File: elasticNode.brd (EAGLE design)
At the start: 82.2 x 52.5 mm, 101 parts, among them J1 ISP_CONN_6PIN, J2 FEMALE_HEADER_2X2, J3 FEMALE_HEADER_2X1, J4 FEMALE_HEADER_2X1, J5 FEMALE_HEADER_5X2, J6 FEMALE_HEADER_5X2, J7 JTAG_CONN_6PINTHT, J8 USB_CONN, U1 ATMEGA64AQFN, U10 LTC3419DFN, U2 SST26VF032B, U3 MRF24J40MA, U4 SPARTAN6-LX9, U5 SST26VF032B, U6 PAC1720, U7 PAC1720, U8 PAC1720, U9 FT232R, X1 12MHz, X2 50MHz, X3 32MHz

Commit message: changed i2c to pullup
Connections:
- removed net N$33: R25.2
- net 3V3: now also R24.2, R25.2
- net GND: no longer R24.2

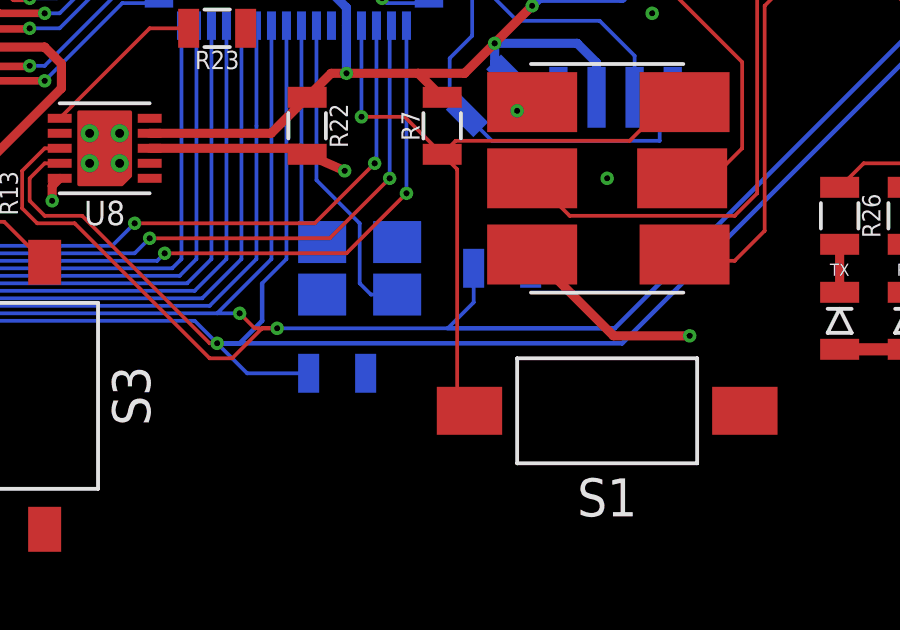
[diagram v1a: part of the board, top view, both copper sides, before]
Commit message: updated board for previous pullups and swapped fpga power rails
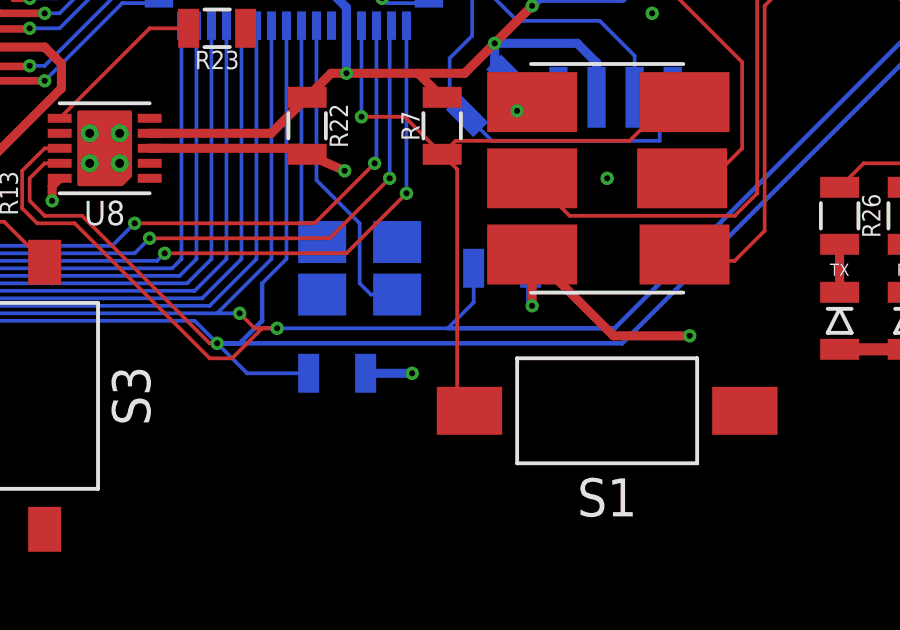
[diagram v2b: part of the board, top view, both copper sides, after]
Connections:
- net 1V2: now also R17.2, U7.3; no longer R19.2, U7.1
- net 3V3: now also R19.2, U7.1; no longer R17.2, U7.3
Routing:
- net 3V3: track 37.6 -> 45.4 mm, vias 11 -> 13
- net 1V2: track 61.3 -> 59.4 mm

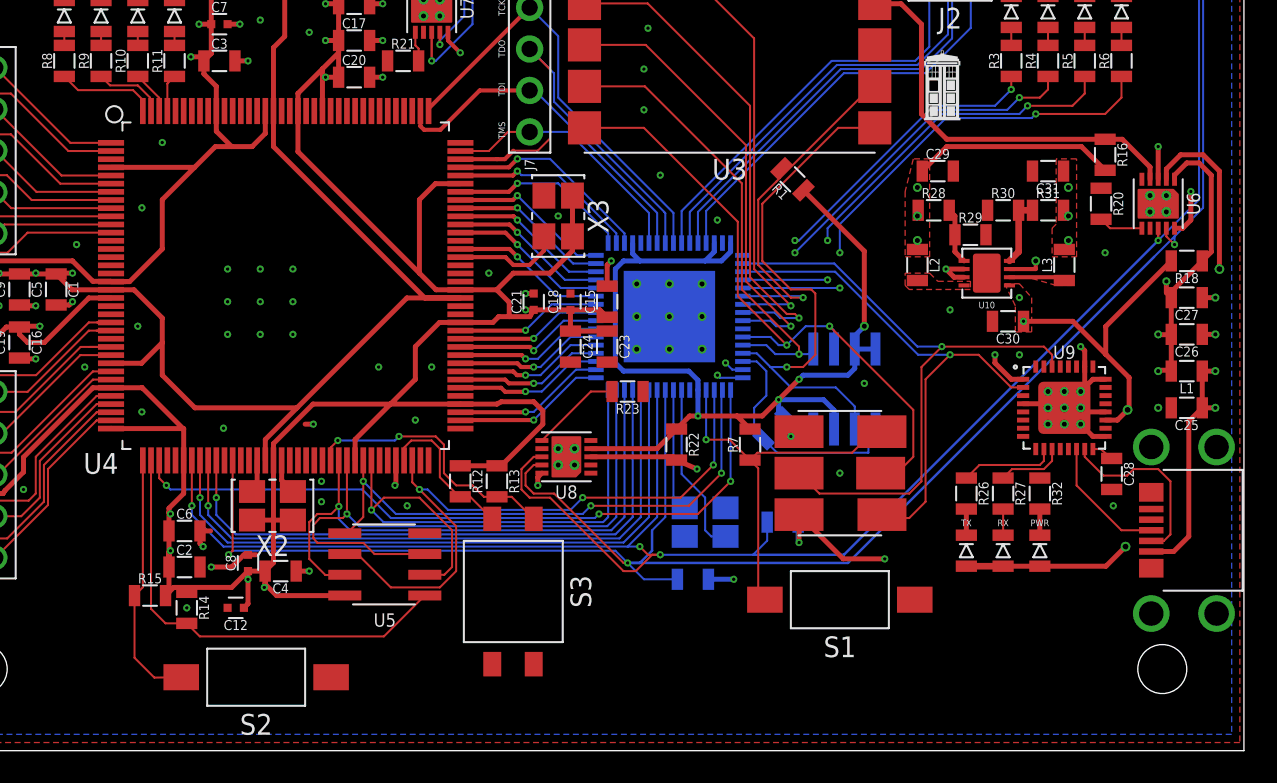
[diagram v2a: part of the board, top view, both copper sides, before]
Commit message: added smd usb connector
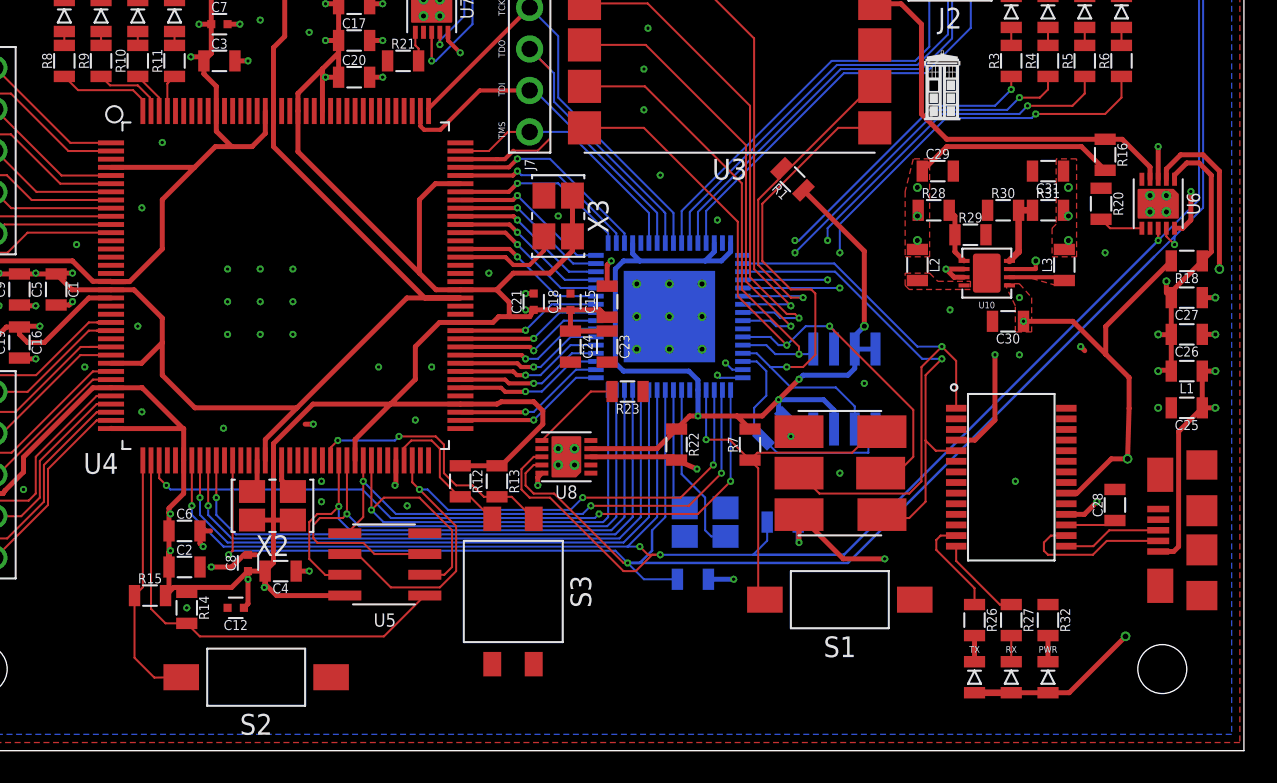
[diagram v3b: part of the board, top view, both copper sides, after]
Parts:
- J8: value USB_CONN -> USB_CONNSMT; device connectors:USB_MICRO_B -> connectors:USB_MICRO_B_SMT
- U9: value FT232R -> FT232RSSOP28; device ic:QFN32 -> ic:SSOP28
- moved PWR 7.77 mm to (70.2, 4.50)
- moved R26 7.77 mm to (65.8, 8.00)
- moved R27 7.77 mm to (68.0, 8.00)
- moved R32 7.77 mm to (70.2, 8.00)
- moved RX 7.77 mm to (68.0, 4.50)
- moved TX 7.77 mm to (65.8, 4.50)
- moved U9 5.35 mm to (68.0, 16.8), turned to 270 degrees
- moved J8 2.75 mm to (77.0, 13.5)
- moved C28 1.91 mm to (74.3, 15.1), turned to 90 degrees
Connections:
- removed net N$17 (its old number): U9.32
- new net N$26: U9.12
- net 12MHZ: now also U9.23; no longer U9.22
- net 5V: now also U9.20, U9.4; no longer U9.1, U9.19
- net FTDI_RXLED: now also U9.14; no longer U9.11
- net GND: now also U9.18, U9.21, U9.25, U9.7; no longer U9.17, U9.20, U9.24, U9.33, U9.4, U9.P$1, U9.P$2, U9.P$3, U9.P$4, U9.P$5, U9.P$6, U9.P$7, U9.P$8, U9.P$9
- net MCU_RX0/PDI: now also U9.1; no longer U9.30
- net MCU_TX0/PDO: now also U9.5; no longer U9.2
- net N$10: now also U9.13; no longer U9.10
- net N$18: now also U9.11; no longer U9.8
- net N$19: now also U9.2; no longer U9.31
- net N$21: now also U9.10; no longer U9.7
- net N$3: now also U9.17; no longer U9.16
- net N$6: now also U9.19; no longer U9.18
- net USBD+: now also U9.15; no longer U9.14
- net USBD-: now also U9.16; no longer U9.15
- net USB_SHIELD: now also J8.CASE_1; no longer J8.SHIELD1
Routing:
- net 5V: track 74.6 -> 87.8 mm
- net GND: track 34.4 -> 26.0 mm, vias 68 -> 69
- net MCU_TX0/PDO: track 32.9 -> 28.9 mm
- net MCU_RX0/PDI: track 39.1 -> 35.5 mm
- net USBD+: track 7.94 -> 6.03 mm
- net USBD-: track 11.3 -> 9.51 mm
- net N$3: track 1.36 -> 3.09 mm
- net FTDI_RXLED: track 4.16 -> 5.38 mm

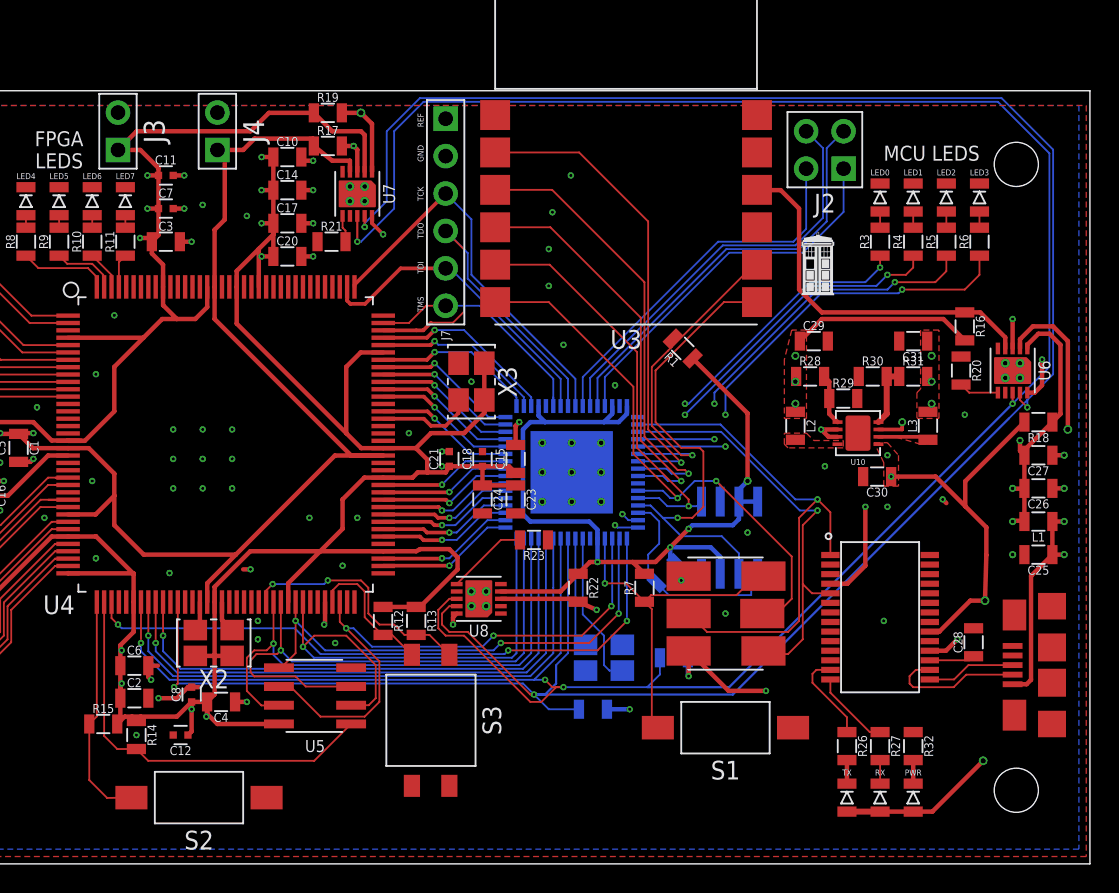
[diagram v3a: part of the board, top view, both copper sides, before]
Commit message: updated footprints, moved reset buttons, general reorganising
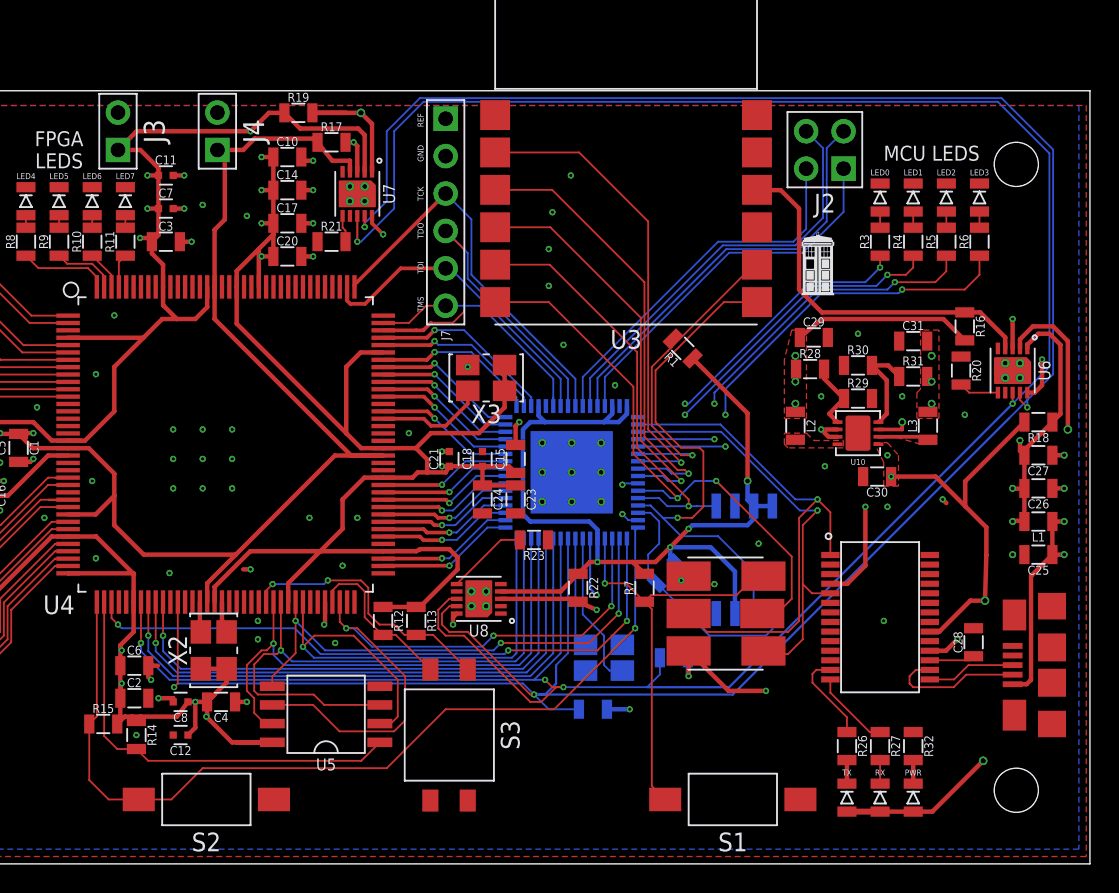
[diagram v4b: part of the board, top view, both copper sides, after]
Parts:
- moved S1 4.90 mm to (58.0, 4.38)
- moved R19 2.00 mm to (28.5, 51.0)
- moved U2 1.80 mm to (58.8, 20.6)
- moved S3 1.60 mm to (38.8, 8.75)
- moved U5 1.46 mm to (30.4, 10.2)
- moved R30 1.25 mm to (66.5, 33.9)
- moved X3 1.03 mm to (41.2, 33.0), turned to 180 degrees
- moved R29 1.00 mm to (66.5, 31.6)
- moved C8 0.90 mm to (20.5, 11.0), turned to 180 degrees
- moved S2 0.52 mm to (22.2, 4.38)
- moved R28 0.50 mm to (63.2, 33.6)
- moved X2 0.50 mm to (22.8, 14.5), turned to 90 degrees
- moved R17 0.35 mm to (30.8, 49.0)
- moved C29 0.25 mm to (63.5, 35.8)
- turned C31 to 0 degrees
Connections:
- removed net MCU_CS: U1.10
- removed net N$38: U1.23, X1.2
- removed net N$39: U1.24, X1.4
- new net XTAL1: U1.24, X1.3
- new net XTAL2: U1.23, X1.1
- net 1V2: now also C31.2; no longer C31.1
- net FPGA_RESET: now also U1.16
- net GND: now also C31.1; no longer C31.2
- net MCU_LED0: now also U1.15; no longer U1.16
- net MCU_LED1: now also U1.10; no longer U1.15
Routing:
- net FPGA_RESET: track 15.7 -> 61.6 mm, vias 0 -> 1
- net XTAL2: track 0.00 -> 10.6 mm
- net N$38: track 10.6 -> 0.00 mm
- net XTAL1: track 0.00 -> 7.50 mm
- net N$39: track 7.50 -> 0.00 mm
- net MCU_RESET: track 24.0 -> 29.1 mm
- net CCLK: track 40.2 -> 44.7 mm
- net MCU_VCC: track 63.4 -> 67.5 mm
- net 3V3: track 45.4 -> 49.2 mm
- net MCU_MISO: track 32.8 -> 35.8 mm
- net SELECTMAP_D1/FPGA_MISO2: track 38.5 -> 41.0 mm
- net N$7: track 4.18 -> 6.66 mm
- net MCU_FLASH_CE: track 14.8 -> 17.0 mm
- net MCU_LED1: track 30.2 -> 28.0 mm
- net GND: track 26.0 -> 28.1 mm, vias 69 -> 73
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
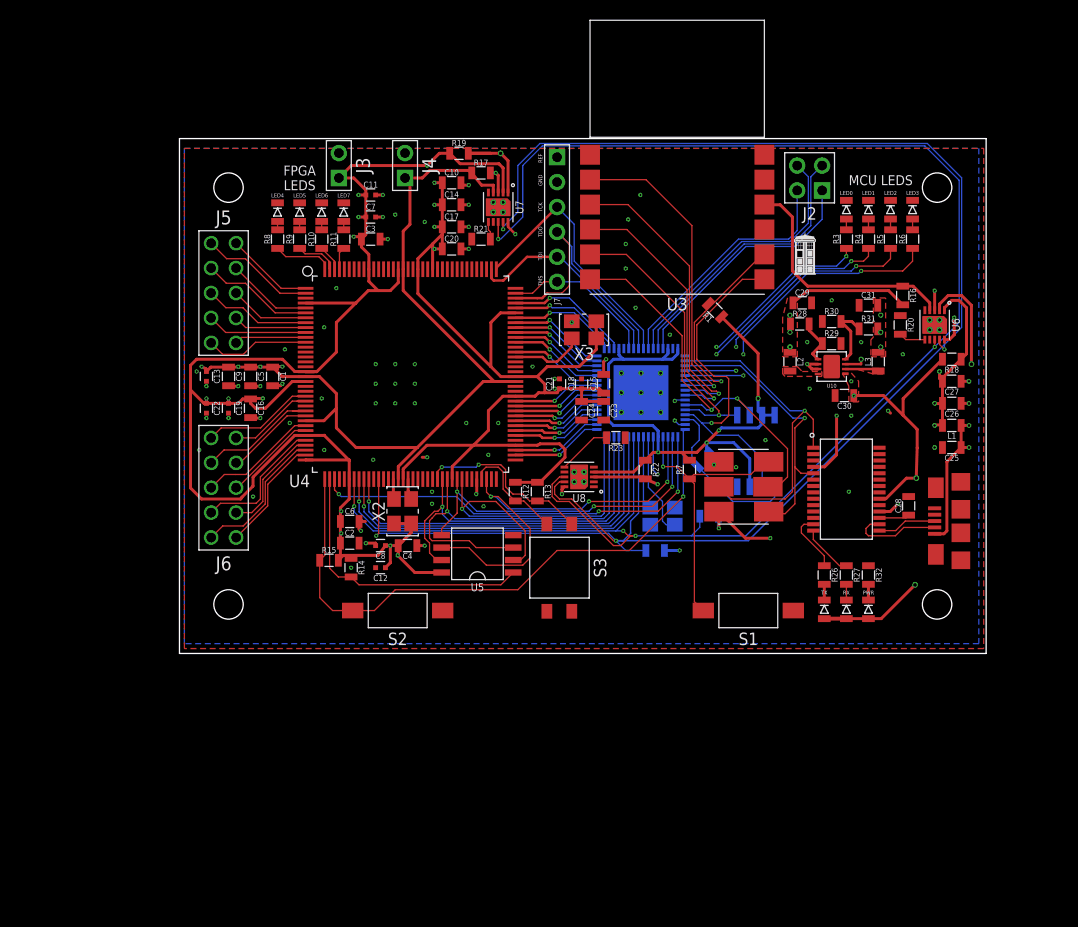
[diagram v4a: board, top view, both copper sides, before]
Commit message: first part toward separate monitoring board
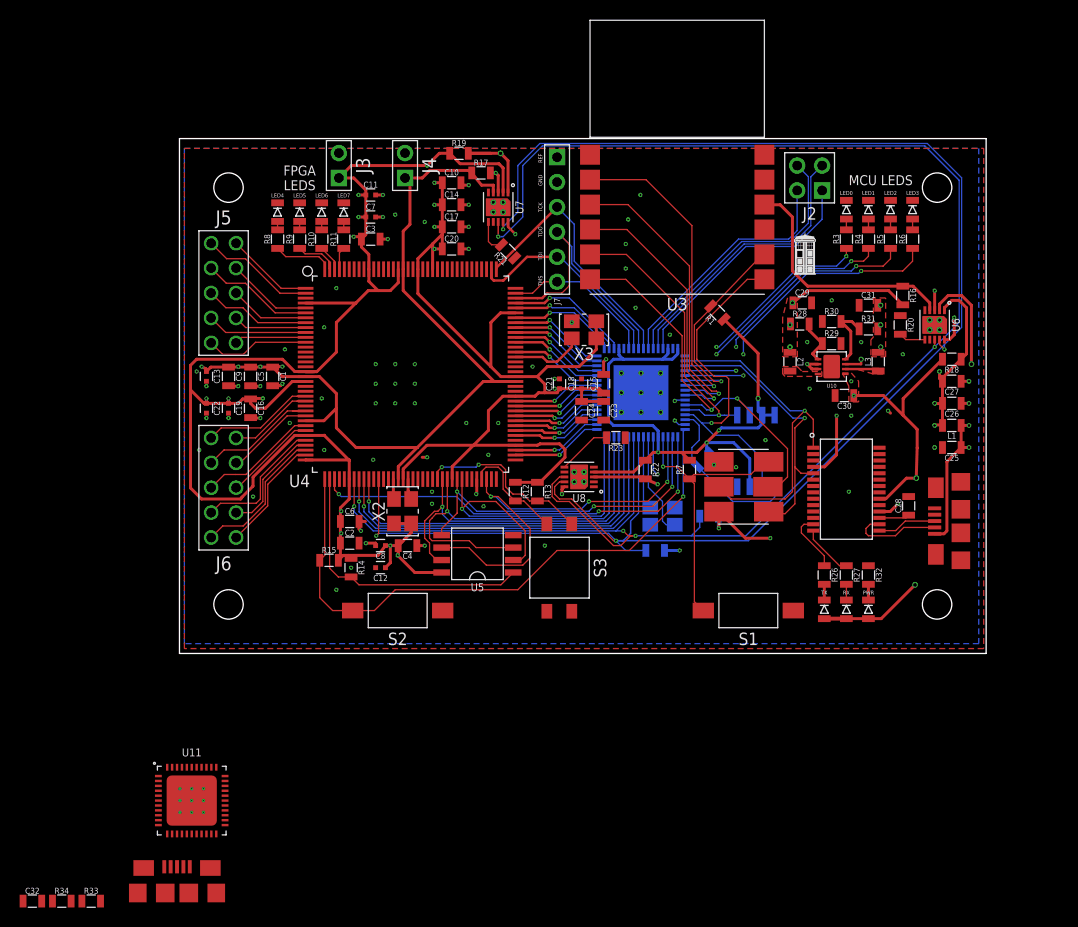
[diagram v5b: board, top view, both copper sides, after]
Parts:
- added C32: 1u, passive:0805
- added J9: USB_CONNSMT, connectors:USB_MICRO_B_SMT
- added R33, R34: 22, passive:0805
- added U11: ATMEGA32U4, ic:QFN44
- moved R21 3.02 mm to (33.5, 41.0), turned to 135 degrees
- moved R1 0.35 mm to (54.9, 34.8)
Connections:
- new net D+: R33.2, U11.4
- new net D-: R34.2, U11.3
- new net N$38: J9.3, R33.1
- new net N$39: J9.2, R34.1
- new net N$43: C32.1, U11.6
- new net N$44: U11.5
- new net USB2_VCC: J9.1, U11.14, U11.2, U11.24, U11.34, U11.44, U11.7
- net GND: now also C32.2, J9.5, U11.15, U11.23, U11.35, U11.43
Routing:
- net N$28: track 1.83 -> 3.46 mm
- net 1V2: track 59.3 -> 58.3 mm
- net GND: vias 73 -> 75
